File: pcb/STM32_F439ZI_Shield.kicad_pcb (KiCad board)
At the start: 2 copper layers, 97 parts, among them CN1 Conn_02x08_Odd_Even, CN2 Conn_02x15_Odd_Even, CN3 Conn_02x10_Odd_Even, CN4 Conn_02x17_Odd_Even, K1 G6S-2, K2 G6S-2, SW1 SW_Push, SW2 SW_Push, SW3 SW_Push, SW4 SW_Push, U1 LM2904, U10 LTV-817S, U11 LTV-817S, U13 R-78E3.3-0.5, U14 R-78E5.0-0.5, U15 ACS724xLCTR-05AB, U2 MAX3485, U3 LTV-817S, U4 LTV-817S, U5 LTV-817S, U6 LTV-817S, U7 LTV-817S, U8 LTV-817S, U9 LTV-817S

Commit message: Save pcb cut out
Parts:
- added ?: , , F.Cu at (200.9, 54.6)
- added ?: , , F.Cu at (249.2, 56.0)
- added ?: , , F.Cu at (202.2, 130.8)
- added ?: , , F.Cu at (247.9, 130.9)
- added ?: , , F.Cu at (233.8, 106.8)
- CN10: renamed from CN4; footprint Connector_PinHeader_2.54mm:PinHeader_2x17_P2.54mm_Vertical_SMD -> Connector_PinHeader_2.54mm:PinHeader_2x17_P2.54mm_Vertical; moved to B.Cu
- CN7: renamed from CN3; footprint Connector_PinHeader_2.54mm:PinHeader_2x10_P2.54mm_Vertical_SMD -> Connector_PinHeader_2.54mm:PinHeader_2x10_P2.54mm_Vertical; moved to B.Cu
- CN8: renamed from CN1; footprint Connector_PinHeader_2.54mm:PinHeader_2x08_P2.54mm_Vertical_SMD -> Connector_PinHeader_2.54mm:PinHeader_2x08_P2.54mm_Vertical; moved to B.Cu
- CN9: renamed from CN2; footprint Connector_PinHeader_2.54mm:PinHeader_2x15_P2.54mm_Vertical_SMD -> Connector_PinHeader_2.54mm:PinHeader_2x15_P2.54mm_Vertical; moved to B.Cu
- moved CN10 180.3 mm to (249.1, 86.4), turned to 180 degrees
- moved CN7 157.9 mm to (249.1, 59.7), turned to 180 degrees
- moved CN9 121.4 mm to (203.5, 91.5), turned to 180 degrees
- moved CN8 120.0 mm to (203.5, 68.6), turned to 180 degrees
- moved Spannungsversorgung_1 58.4 mm to (139.7, 27.7), turned to 180 degrees
- moved Motor_Leistungsversorgung_1 55.1 mm to (168.0, 25.7), turned to 180 degrees
- moved Motor_Logik_1 49.6 mm to (170.3, 65.0)
- moved Enschalter_Hinten_1 42.4 mm to (134.5, 157.7), turned to -90 degrees
- moved Abstandssensor_1 36.1 mm to (88.6, 25.1), turned to -90 degrees
- moved Anemometer_1 35.1 mm to (79.1, 73.3), turned to -90 degrees
- moved Kraftsensor_1 21.2 mm to (52.1, 54.9), turned to 180 degrees
- moved Enschalter_Vorne_1 3.07 mm to (108.0, 141.8), turned to -90 degrees
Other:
- board outline added: 70 x 133.4 mm

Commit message: updated pcb
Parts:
- removed the ? at (233.8, 106.8)
- removed Abstandssensor_1, Enschalter_Hinten_1, Enschalter_Vorne_1: Conn_01x04_Pin, Connector_Phoenix_MSTB:PhoenixContact_MSTBA_2,5_4-G-5,08_1x04_P5.08mm_Horizontal
- removed Anemometer_1: Conn_01x08_Pin, Connector_Phoenix_MSTB:PhoenixContact_MSTBA_2,5_8-G-5,08_1x08_P5.08mm_Horizontal
- removed Motor_Leistungsversorgung_1: Conn_01x03_Pin, Connector_Phoenix_MSTB:PhoenixContact_MSTBA_2,5_3-G_1x03_P5.00mm_Horizontal
- removed Motor_Logik_1: Conn_02x06_Counter_Clockwise, Connector_PinHeader_2.54mm:PinHeader_2x06_P2.54mm_Vertical_SMD
- removed SW1, SW2, SW3, SW4: SW_Push, Button_Switch_THT:SW_PUSH_6mm_H4.3mm
- removed U14: R-78E5.0-0.5, Converter_DCDC:Converter_DCDC_RECOM_R-78E-0.5_THT
- added Abstandssensor1: Conn_01x03_Pin, TerminalBlock_TE-Connectivity:TerminalBlock_TE_282834-3_1x03_P2.54mm_Horizontal, F.Cu at (147.0, 154.0)
- added Anenometer1: Conn_01x07_Pin, TerminalBlock_TE-Connectivity:TerminalBlock_TE_282834-7_1x07_P2.54mm_Horizontal, F.Cu at (137.9, 154.0)
- added D14: LED_Gelb, LED_SMD:LED_1206_3216Metric, F.Cu at (150.3, 113.7)
- added D15: LED_Gelb, LED_SMD:LED_1206_3216Metric, F.Cu at (143.4, 113.7)
- added D16: LED_Green, LED_SMD:LED_1206_3216Metric, F.Cu at (138.8, 128.5)
- added Endschalter_Hinten1: Conn_01x03_Pin, TerminalBlock_TE-Connectivity:TerminalBlock_TE_282834-3_1x03_P2.54mm_Horizontal, F.Cu at (154.5, 27.6)
- added Endschalter_Vorne1: Conn_01x03_Pin, TerminalBlock_TE-Connectivity:TerminalBlock_TE_282834-3_1x03_P2.54mm_Horizontal, F.Cu at (165.2, 27.5)
- added J1: Conn_01x02_Pin, Connector_PinHeader_2.54mm:PinHeader_2x01_P2.54mm_Vertical_SMD, F.Cu at (130.7, 99.8)
- added J3: Relais_Conn, TerminalBlock_TE-Connectivity:TerminalBlock_TE_282834-2_1x02_P2.54mm_Horizontal, F.Cu at (169.1, 154.0)
- added J4: Conn_01x02_Pin, TerminalBlock_TE-Connectivity:TerminalBlock_TE_282834-2_1x02_P2.54mm_Horizontal, F.Cu at (170.5, 63.2)
- added J5: Conn_01x02_Pin, TerminalBlock_TE-Connectivity:TerminalBlock_TE_282834-2_1x02_P2.54mm_Horizontal, F.Cu at (170.5, 74.5)
- added J6: Conn_01x02_Pin, Connector_PinHeader_2.54mm:PinHeader_2x01_P2.54mm_Vertical_SMD, F.Cu at (130.7, 95.3)
- added J7: Conn_01x02_Pin, Connector_PinHeader_2.54mm:PinHeader_2x01_P2.54mm_Vertical_SMD, F.Cu at (130.7, 89.4)
- added J8: Conn_01x02_Pin, Connector_PinHeader_2.54mm:PinHeader_2x01_P2.54mm_Vertical_SMD, F.Cu at (130.7, 83.5)
- added Motor_Logik1: Conn_01x10_Pin, TerminalBlock_TE-Connectivity:TerminalBlock_TE_1-282834-0_1x10_P2.54mm_Horizontal, F.Cu at (119.7, 27.5)
- added Motor_Spannungsversorgung1: Conn_01x02_Pin, TerminalBlock_TE-Connectivity:TerminalBlock_TE_282834-2_1x02_P2.54mm_Horizontal, F.Cu at (108.4, 154.0)
- added R41: 2300, Resistor_SMD:R_1206_3216Metric, F.Cu at (152.8, 123.3)
- added R42: 1000, Resistor_SMD:R_1206_3216Metric, F.Cu at (155.1, 123.3)
- added R43: 150, Resistor_SMD:R_1206_3216Metric, F.Cu at (167.9, 70.1)
- C10: value 220n -> 22n
- D1, D2, D3, D4, D5, D6, D7, D8, D9: footprint Diode_SMD:D_SMB -> Diode_SMD:D_SOD-123
- Kraftmessung1: renamed from Kraftsensor_1; footprint Connector_Phoenix_MSTB:PhoenixContact_MSTBA_2,5_4-G-5,08_1x04_P5.08mm_Horizontal -> TerminalBlock_TE-Connectivity:TerminalBlock_TE_282834-3_1x03_P2.54mm_Horizontal
- R2: value 2300 -> 10k
- R25: value 2,2k -> 36k
- R26: value 6,8k -> 120
- R27: value 2,2k -> 120
- R28: value 6,8k -> 150
- R3: value 1000 -> 10k
- R33, R35: value 10k -> 700
- R34, R36: value 36k -> 11k
- Spannungsversorgung_1: footprint Connector_Phoenix_MSTB:PhoenixContact_MSTBA_2,5_2-G-5,08_1x02_P5.08mm_Horizontal -> TerminalBlock_TE-Connectivity:TerminalBlock_TE_282834-2_1x02_P2.54mm_Horizontal
- moved Kraftmessung1 143.6 mm to (156.1, 154.0)
- moved R34 108.0 mm to (169.9, 148.9)
- moved R36 101.0 mm to (164.3, 148.9), turned to 180 degrees
- moved D2 100.3 mm to (159.3, 32.5)
- moved D1 97.4 mm to (166.9, 32.5), turned to 180 degrees
- moved R33 96.0 mm to (171.0, 133.4), turned to -90 degrees
- moved R1 91.7 mm to (155.1, 117.9), turned to 90 degrees
- moved R35 88.9 mm to (165.4, 133.4), turned to -90 degrees
- moved CN10 86.1 mm to (163.0, 83.8)
- moved ? 86.1 mm to (114.8, 52.0)
- moved ? 86.1 mm to (163.1, 53.3)
- moved ? 86.1 mm to (116.1, 128.2)
- moved ? 86.1 mm to (161.8, 128.2)
- moved CN7 86.1 mm to (163.0, 57.0)
- moved CN8 86.1 mm to (117.4, 66.0)
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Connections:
- C10 pad 1: /Buttons/MCU_Button4 -> /STM32F439ZI/Opt_Temperaturmessung
- C7 pad 1: /Buttons/MCU_Button1 -> /Buttons_LEDS/MCU_Vorfahren
- C8 pad 1: /Buttons/MCU_Button2 -> /Buttons_LEDS/MCU_Zurueckfahren
- C9 pad 1: /Buttons/MCU_Button3 -> /Buttons_LEDS/MCU_Kalibrierung
- CN10 pad 10: unconnected-(CN10-Pin_10-Pad10) -> /Buttons_LEDS/MCU_LED_PWR
- CN10 pad 12: unconnected-(CN10-Pin_12-Pad12) -> /Buttons_LEDS/MCU_LED_Betrieb
- CN10 pad 14: unconnected-(CN10-Pin_14-Pad14) -> /Buttons_LEDS/MCU_LED_Manuell
- CN10 pad 16: unconnected-(CN10-Pin_16-Pad16) -> /Buttons_LEDS/MCU_LED_Stoerung
- CN10 pad 18: unconnected-(CN10-Pin_18-Pad18) -> /Buttons_LEDS/MCU_LED_Kalibrierung
- CN10 pad 2: unconnected-(CN10-Pin_2-Pad2) -> /Buttons_LEDS/MCU_Vorfahren
- CN10 pad 20: unconnected-(CN10-Pin_20-Pad20) -> /Buttons_LEDS/MCU_LED_Rollen
- CN10 pad 22: unconnected-(CN10-Pin_22-Pad22) -> /Buttons_LEDS/MCU_LED_Trimmen
- CN10 pad 30: unconnected-(CN10-Pin_30-Pad30) -> /STM32F439ZI/Abstandsmessung_MCU
- CN10 pad 32: unconnected-(CN10-Pin_32-Pad32) -> /STM32F439ZI/Kraftmessung_MCU
- CN10 pad 33: unconnected-(CN10-Pin_33-Pad33) -> /Optokoppler/Ext_Relais1_MCU
- CN10 pad 34: unconnected-(CN10-Pin_34-Pad34) -> /Optokoppler/Ext_Relais2_MCU
- CN10 pad 4: unconnected-(CN10-Pin_4-Pad4) -> /Buttons_LEDS/MCU_Zurueckfahren
- CN10 pad 6: unconnected-(CN10-Pin_6-Pad6) -> /Buttons_LEDS/MCU_Kalibrierung
- CN10 pad 8: unconnected-(CN10-Pin_8-Pad8) -> /Buttons_LEDS/MCU_Switch
- CN7 pad 1: unconnected-(CN7-Pin_1-Pad1) -> /STM32F439ZI/Endschalter_Vorne_MCU
- CN7 pad 11: unconnected-(CN7-Pin_11-Pad11) -> /STM32F439ZI/Opt_Analog_IN
- CN7 pad 18: unconnected-(CN7-Pin_18-Pad18) -> /STM32F439ZI/Drehzahl_Analog_OUT
- CN7 pad 2: unconnected-(CN7-Pin_2-Pad2) -> /STM32F439ZI/IN1_MCU
- CN7 pad 3: unconnected-(CN7-Pin_3-Pad3) -> /STM32F439ZI/IN0_MCU
- CN7 pad 4: unconnected-(CN7-Pin_4-Pad4) -> /STM32F439ZI/Endschalter_Hinten_MCU
- CN7 pad 9: unconnected-(CN7-Pin_9-Pad9) -> /STM32F439ZI/Opt_Temperaturmessung
- CN8 pad 11: unconnected-(CN8-Pin_11-Pad11) -> /Optokoppler/IN2_MCU_IN
- CN8 pad 3: unconnected-(CN8-Pin_3-Pad3) -> /Optokoppler/OUT1_MCU
- CN8 pad 5: unconnected-(CN8-Pin_5-Pad5) -> /Optokoppler/OUT2_MCU
- CN8 pad 7: unconnected-(CN8-Pin_7-Pad7) -> /Optokoppler/OUT3_MCU
- CN8 pad 8: unconnected-(CN8-Pin_8-Pad8) -> +3.3V
- CN8 pad 9: unconnected-(CN8-Pin_9-Pad9) -> /Optokoppler/IN3_MCU_IN
- CN9 pad 16: unconnected-(CN9-Pin_16-Pad16) -> /Motor/Stromsensor_MCU
- CN9 pad 2: unconnected-(CN9-Pin_2-Pad2) -> /Rx
- CN9 pad 25: unconnected-(CN9-Pin_25-Pad25) -> /STM32F439ZI/Windrichtung_MCU
- CN9 pad 27: unconnected-(CN9-Pin_27-Pad27) -> /STM32F439ZI/Windgeschwindigkeit_MCU
- CN9 pad 3: unconnected-(CN9-Pin_3-Pad3) -> /Enable
- CN9 pad 5: unconnected-(CN9-Pin_5-Pad5) -> /Tx
- D1 pad 1: /Endschalter/Endschalter_Vorne_IN_1 -> /Endschalter/Endschalter_Vorne
- D2 pad 1: /Endschalter/Endschalter_Hinten_IN_1 -> /Endschalter/Endschalter_Hinten
- D3 pad 1: /Motor/IN0_OUT -> /Motor/IN3_OUT
- D4 pad 1: /Motor/IN1_OUT -> /Motor/OUT3_IN
- D5 pad 1: /Motor/IN2_OUT -> /Motor/OUT2_IN
- D6 pad 1: /Motor/IN3_OUT -> /Motor/OUT1_IN
- D7 pad 1: /Motor/OUT3_IN -> /Motor/IN0_OUT
- D8 pad 1: /Motor/OUT2_IN -> /Motor/IN1_OUT
- D9 pad 1: /Motor/OUT1_IN -> /Motor/IN2_OUT
- K1 pad 1: /Endschalter/Endschalter_Hinten_IN_1 -> /Endschalter/Endschalter_Hinten
- K1 pad 3: /STM32F439ZI/IN1_MCU -> /Optokoppler/IN1_MCU_IN
- K1 pad 4: /Optokoppler/IN1_MCU_IN -> /STM32F439ZI/IN1_MCU
- K1 pad 5: unconnected-(K1-Pad5) -> /STM32F439ZI/Endschalter_Hinten_MCU
- K2 pad 1: /Endschalter/Endschalter_Vorne_IN_1 -> /Endschalter/Endschalter_Vorne
- K2 pad 3: /STM32F439ZI/IN0_MCU -> /Optokoppler/IN0_MCU_IN
- K2 pad 4: /Optokoppler/IN0_MCU_IN -> /STM32F439ZI/IN0_MCU
- K2 pad 5: unconnected-(K2-Pad5) -> /STM32F439ZI/Endschalter_Vorne_MCU
- Kraftmessung1 pad 2: Net-(Kraftsensor_1-Pin_2) -> GND
- Kraftmessung1 pad 3: GND -> Net-(Kraftmessung1-Pin_3)
- R14 pad 1: Net-(R14-Pad1) -> /Motor/IN1_OUT
- R19 pad 1: /Motor/OUT3_IN -> /Motor/OUT1_IN
- R2 pad 1: Net-(Kraftsensor_1-Pin_2) -> GND
- R2 pad 2: /STM32F439ZI/Kraftmessung_MCU -> /Buttons_LEDS/MCU_Switch
- R23 pad 1: /Motor/OUT1_IN -> /Motor/OUT3_IN
- R25 pad 1: /Endschalter/Endschalter_Vorne_IN_1 -> Net-(J6-Pin_1)
- R25 pad 2: Net-(R25-Pad2) -> /Buttons_LEDS/MCU_Kalibrierung
- R26 pad 1: /Optokoppler/Endschalter_Vorne_MCU -> /Buttons_LEDS/MCU_LED_Trimmen
- R26 pad 2: GND -> Net-(D14-A)
- R27 pad 1: /Endschalter/Endschalter_Hinten_IN_1 -> /Buttons_LEDS/MCU_LED_Rollen
- R27 pad 2: Net-(R27-Pad2) -> Net-(D15-A)
- R28 pad 1: /Optokoppler/Endschalter_Hinten_MCU -> /Buttons_LEDS/MCU_LED_Kalibrierung
- R28 pad 2: GND -> Net-(D16-A)
- R3 pad 1: /STM32F439ZI/Kraftmessung_MCU -> +3.3V
- R3 pad 2: GND -> Net-(J6-Pin_1)
- R30 pad 2: /Buttons/MCU_Button1 -> /Buttons_LEDS/MCU_Vorfahren
- R32 pad 2: /Buttons/MCU_Button2 -> /Buttons_LEDS/MCU_Zurueckfahren
- R33 pad 1: +3.3V -> /Optokoppler/Ext_Relais1_MCU
- R34 pad 1: Net-(R33-Pad2) -> /Optokoppler/Ext_Relais1_OUT
- R34 pad 2: /Buttons/MCU_Button3 -> GND
- R35 pad 1: +3.3V -> /Optokoppler/Ext_Relais2_MCU
- R36 pad 1: Net-(R35-Pad2) -> /Optokoppler/Ext_Relais2_OUT
- R36 pad 2: /Buttons/MCU_Button4 -> GND
- R37 pad 1: /Buttons/MCU_LED_Red -> /Buttons_LEDS/MCU_LED_Stoerung
- R38 pad 1: /Buttons/MCU_LED_Gelb -> /Buttons_LEDS/MCU_LED_Manuell
- R39 pad 1: /Buttons/MCU_LED_Green2 -> /Buttons_LEDS/MCU_LED_Betrieb
- R4 pad 1: /STM32F439ZI/Windrichtung_MCU -> /STM32F439ZI/Windgeschwindigkeit_MCU
- R40 pad 1: /Buttons/MCU_LED_Green1 -> /Buttons_LEDS/MCU_LED_PWR
- R5 pad 1: /STM32F439ZI/Windgeschwindigkeit_MCU -> /STM32F439ZI/Windrichtung_MCU
- U10 pad 1: Net-(R25-Pad2) -> Net-(R33-Pad2)
- U10 pad 3: /Optokoppler/Endschalter_Vorne_MCU -> /Optokoppler/Ext_Relais1_OUT
- U10 pad 4: +3.3V -> +24V
- U11 pad 1: Net-(R27-Pad2) -> Net-(R35-Pad2)
- U11 pad 3: /Optokoppler/Endschalter_Hinten_MCU -> /Optokoppler/Ext_Relais2_OUT
- U11 pad 4: +3.3V -> +24V
- U15 pad 8: +5V -> +3.3V
- U4 pad 3: Net-(R14-Pad1) -> /Motor/IN1_OUT
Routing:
- net +24V: track 0.00 -> 325.4 mm, vias 0 -> 4
- net +3.3V: track 0.00 -> 155.3 mm
- net GND: track 0.00 -> 121.5 mm, vias 0 -> 36
- net /Rx: track 0.00 -> 64.0 mm
- net /Optokoppler/IN3_MCU_IN: track 0.00 -> 58.6 mm
- net /Enable: track 0.00 -> 55.2 mm
- net /Optokoppler/IN2_MCU_IN: track 0.00 -> 54.3 mm
- net /Motor/OUT3_IN: track 0.00 -> 52.4 mm
- net /Motor/Drehzahl_Analog_OUT: track 0.00 -> 52.1 mm
- net /Tx: track 0.00 -> 50.9 mm
- net /STM32F439ZI/Abstandsmessung_MCU: track 0.00 -> 47.0 mm
- net /Motor/OUT2_IN: track 0.00 -> 42.3 mm
- net /STM32F439ZI/Windrichtung_MCU: track 0.00 -> 38.8 mm
- net /Motor/Stromsensor_MCU: track 0.00 -> 38.7 mm
- net /Motor/OUT1_IN: track 0.00 -> 36.9 mm
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- added copper zone on B.Cu, net GND
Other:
- outline, holes or cut-outs redrawn
- board text added: "Endschalter_Hinten"
- board text added: "Endschalter_Vorne"
- board text added: "Motor_Spannungsversorgung"
- board text added: "Spannungsversorgung"
- board text added: "kraftsensor"

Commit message: finished PCB Design V1.0
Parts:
- moved D15 33.9 mm to (168.7, 91.1), turned to 180 degrees
- moved R39 28.7 mm to (128.4, 103.1)
- moved D10 28.1 mm to (148.4, 97.1)
- moved R28 19.6 mm to (140.0, 114.9)
- moved D14 18.4 mm to (168.7, 114.5), turned to 180 degrees
- moved R38 15.8 mm to (141.1, 103.1)
- moved D13 12.9 mm to (150.5, 109.0)
- moved R27 11.7 mm to (166.0, 100.1), turned to 90 degrees
- moved R26 10.3 mm to (166.0, 105.5), turned to -90 degrees
- moved D16 8.16 mm to (138.6, 120.4)
- moved D12 6.44 mm to (138.6, 109.0)
- moved D11 5.69 mm to (126.9, 109.0)
- moved R37 4.87 mm to (152.0, 103.7)
- moved R40 2.55 mm to (156.3, 91.4)
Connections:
- CN10 pad 10: /Buttons_LEDS/MCU_LED_PWR -> /Buttons_LEDS/MCU_LED_Betrieb
- CN10 pad 12: /Buttons_LEDS/MCU_LED_Betrieb -> /Buttons_LEDS/MCU_LED_Manuell
- CN10 pad 14: /Buttons_LEDS/MCU_LED_Manuell -> /Buttons_LEDS/MCU_LED_Stoerung
- CN10 pad 15: unconnected-(CN10-Pin_15-Pad15) -> /Buttons_LEDS/MCU_LED_Rollen
- CN10 pad 16: /Buttons_LEDS/MCU_LED_Stoerung -> /Buttons_LEDS/MCU_LED_Kalibrierung
- CN10 pad 17: unconnected-(CN10-Pin_17-Pad17) -> /Buttons_LEDS/MCU_LED_Trimmen
- CN10 pad 18: /Buttons_LEDS/MCU_LED_Kalibrierung -> unconnected-(CN10-Pin_18-Pad18)
- CN10 pad 2: /Buttons_LEDS/MCU_Vorfahren -> /Buttons_LEDS/MCU_Zurueckfahren
- CN10 pad 20: /Buttons_LEDS/MCU_LED_Rollen -> unconnected-(CN10-Pin_20-Pad20)
- CN10 pad 22: /Buttons_LEDS/MCU_LED_Trimmen -> unconnected-(CN10-Pin_22-Pad22)
- CN10 pad 4: /Buttons_LEDS/MCU_Zurueckfahren -> /Buttons_LEDS/MCU_Kalibrierung
- CN10 pad 6: /Buttons_LEDS/MCU_Kalibrierung -> /Buttons_LEDS/MCU_Switch
- CN10 pad 8: /Buttons_LEDS/MCU_Switch -> /Buttons_LEDS/MCU_LED_PWR
- CN7 pad 20: unconnected-(CN7-Pin_20-Pad20) -> /Buttons_LEDS/MCU_Vorfahren
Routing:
- net +3.3V: track 155.3 -> 286.3 mm
- net /Buttons_LEDS/MCU_LED_Betrieb: track 2.68 -> 34.4 mm
- net /Buttons_LEDS/MCU_LED_Kalibrierung: track 2.68 -> 28.3 mm
- net /Buttons_LEDS/MCU_LED_Manuell: track 2.68 -> 20.7 mm
- net GND: track 121.5 -> 135.0 mm, vias 36 -> 40
- net Net-(D10-A): track 18.0 -> 8.21 mm
- net /Buttons_LEDS/MCU_LED_Stoerung: track 2.68 -> 11.2 mm
- net Net-(D14-A): track 0.00 -> 8.05 mm
- net /Optokoppler/Ext_Relais2_OUT: track 3.92 -> 9.26 mm
- net Net-(D15-A): track 3.03 -> 8.09 mm
- net Net-(D12-A): track 7.76 -> 4.84 mm
- net Net-(D13-A): track 6.62 -> 3.87 mm
- net Net-(D11-A): track 6.81 -> 4.51 mm
- net /Buttons_LEDS/MCU_Vorfahren: track 30.7 -> 32.3 mm
- net /Buttons_LEDS/MCU_Zurueckfahren: track 29.5 -> 30.5 mm
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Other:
- outline, holes or cut-outs redrawn

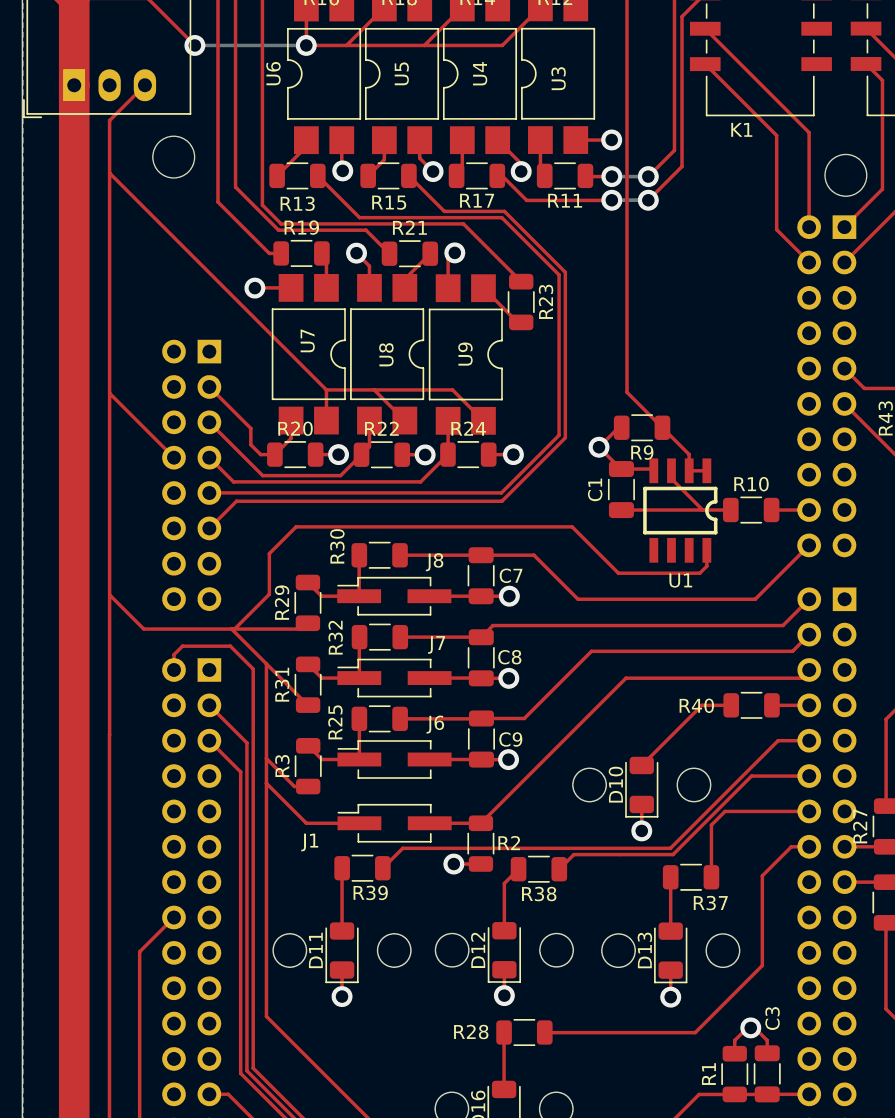
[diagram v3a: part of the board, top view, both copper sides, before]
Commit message: added voltage regulator updated pinout
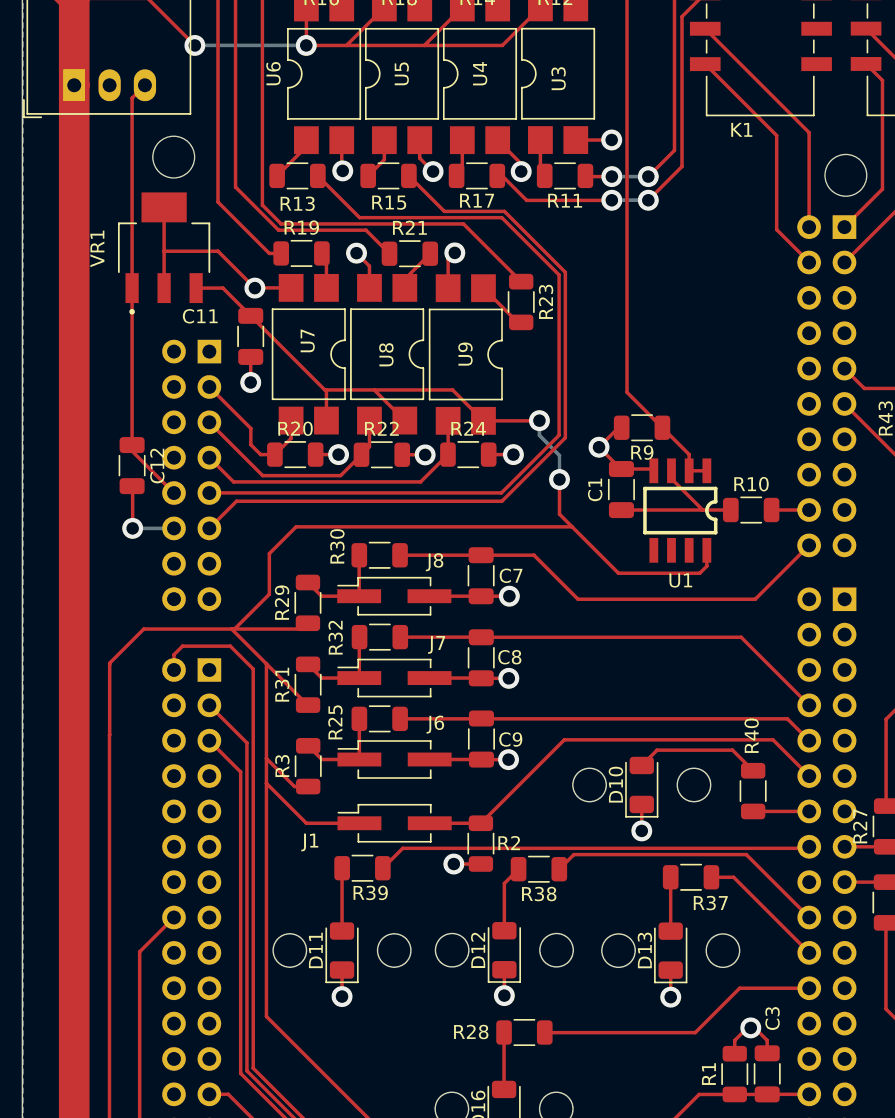
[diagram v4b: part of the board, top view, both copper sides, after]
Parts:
- added C11: 33uF, Capacitor_SMD:C_1206_3216Metric, F.Cu at (120.3, 64.9)
- added C12: 0.47uF, Capacitor_SMD:C_1206_3216Metric, F.Cu at (111.8, 74.2)
- added VR1: LM3940IMP-3.3/NOPB, LM3940IMP-3.3_NOPB:VREG_LM3940IMP-3.3_NOPB, F.Cu at (114.1, 58.5)
- U13: value R-78E3.3-0.5 -> R-78E-5.0-1.0
- moved R40 6.16 mm to (156.4, 97.5), turned to 90 degrees
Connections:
- CN10 pad 10: /Buttons_LEDS/MCU_LED_Betrieb -> /Buttons_LEDS/MCU_Kalibrierung
- CN10 pad 12: /Buttons_LEDS/MCU_LED_Manuell -> /Buttons_LEDS/MCU_Switch
- CN10 pad 14: /Buttons_LEDS/MCU_LED_Stoerung -> /Buttons_LEDS/MCU_LED_PWR
- CN10 pad 16: /Buttons_LEDS/MCU_LED_Kalibrierung -> /Buttons_LEDS/MCU_LED_Betrieb
- CN10 pad 2: /Buttons_LEDS/MCU_Zurueckfahren -> unconnected-(CN10-Pin_2-Pad2)
- CN10 pad 20: unconnected-(CN10-Pin_20-Pad20) -> /Buttons_LEDS/MCU_LED_Manuell
- CN10 pad 22: unconnected-(CN10-Pin_22-Pad22) -> /Buttons_LEDS/MCU_LED_Stoerung
- CN10 pad 24: unconnected-(CN10-Pin_24-Pad24) -> /Buttons_LEDS/MCU_LED_Kalibrierung
- CN10 pad 4: /Buttons_LEDS/MCU_Kalibrierung -> unconnected-(CN10-Pin_4-Pad4)
- CN10 pad 6: /Buttons_LEDS/MCU_Switch -> unconnected-(CN10-Pin_6-Pad6)
- CN10 pad 8: /Buttons_LEDS/MCU_LED_PWR -> /Buttons_LEDS/MCU_Zurueckfahren
- CN8 pad 10: unconnected-(CN8-Pin_10-Pad10) -> +5V
- CN8 pad 12: unconnected-(CN8-Pin_12-Pad12) -> GND
- CN8 pad 8: +3.3V -> unconnected-(CN8-Pin_8-Pad8)
- U13 pad 3: +3.3V -> +5V
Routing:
- net +3.3V: track 286.3 -> 240.2 mm, vias 0 -> 2
- net +5V: track 0.00 -> 30.9 mm
- net GND: track 135.0 -> 156.3 mm, vias 40 -> 42
- net /Buttons_LEDS/MCU_LED_Kalibrierung: track 28.3 -> 20.3 mm
- net /Buttons_LEDS/MCU_LED_Betrieb: track 34.4 -> 31.3 mm
- net /Buttons_LEDS/MCU_LED_Stoerung: track 11.2 -> 9.28 mm
- net /Buttons_LEDS/MCU_Kalibrierung: track 31.9 -> 30.1 mm
- net /Buttons_LEDS/MCU_LED_PWR: track 2.68 -> 4.03 mm
- net /Buttons_LEDS/MCU_Switch: track 31.8 -> 30.8 mm
- net /Buttons_LEDS/MCU_Zurueckfahren: track 30.5 -> 31.4 mm
- net Net-(D10-A): track 8.21 -> 9.07 mm
